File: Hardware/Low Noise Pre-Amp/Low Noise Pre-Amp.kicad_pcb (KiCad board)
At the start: 2 copper layers, 100 x 50 mm, 58 parts, among them J1 RF2-152-T-00-50-G-HDW, J2 RF2-152-T-00-50-G-HDW, J3 RF2-152-T-00-50-G-HDW, J4 WM4111-ND, U1 ADA4841-2, U2 LTC3260xMSE, U3 ADA4841-2, U4 L78L05_SOT89, U5 L79L05

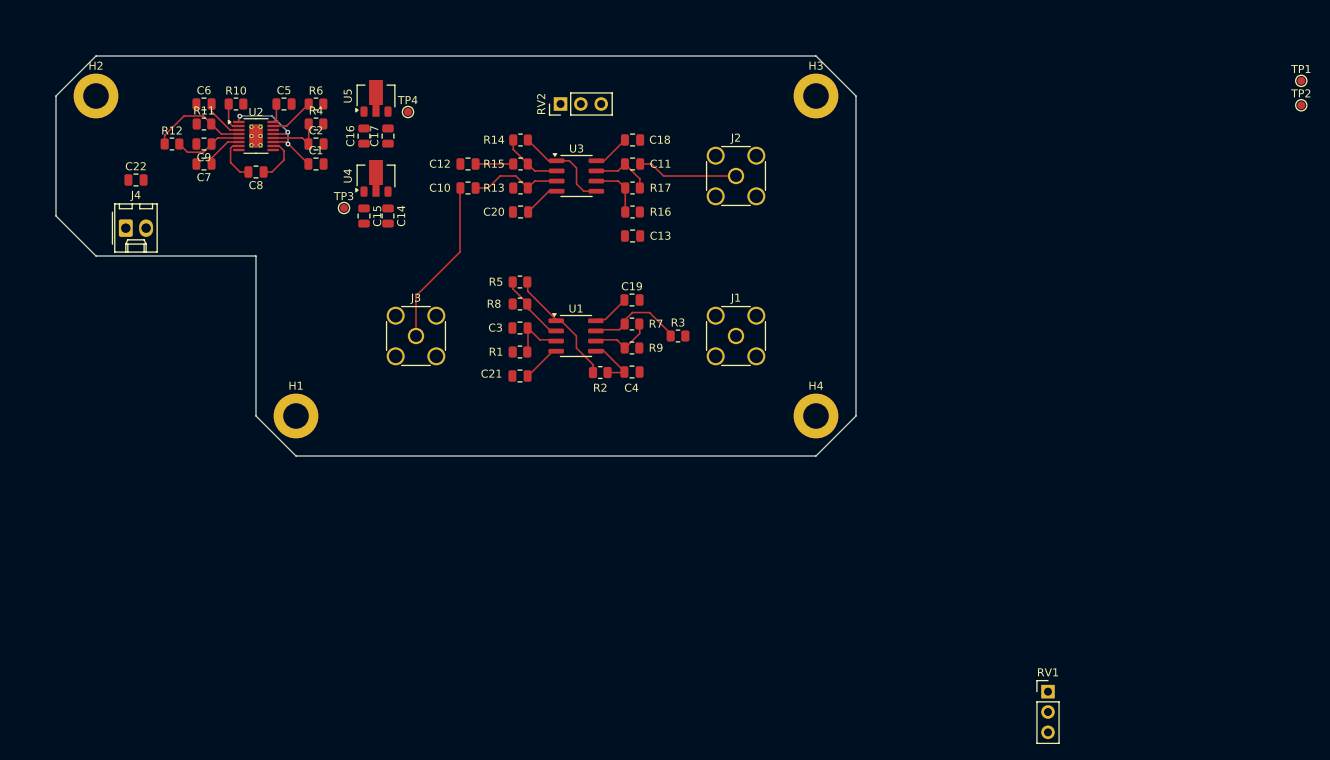
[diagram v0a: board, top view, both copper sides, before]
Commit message: Finalizing board layout
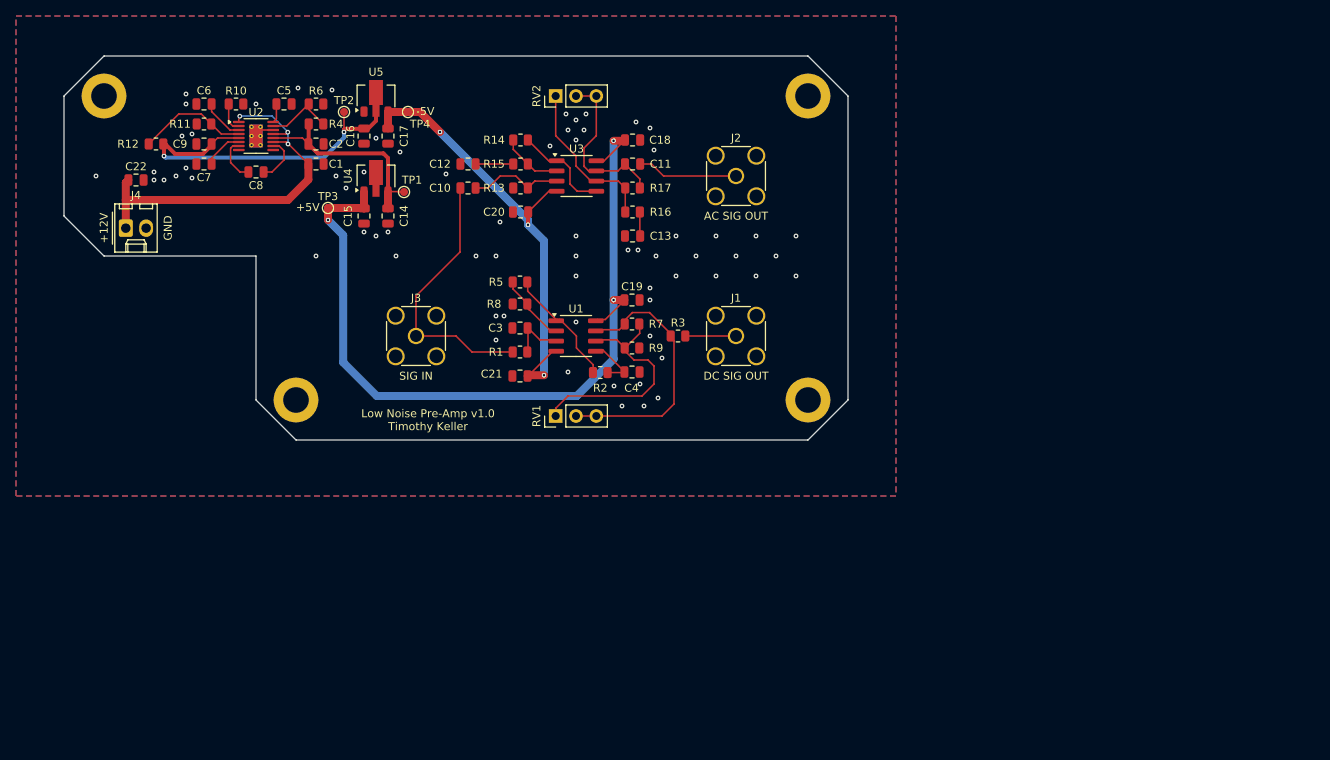
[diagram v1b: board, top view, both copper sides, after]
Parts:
- moved TP2 119.7 mm to (86.0, 57.0)
- moved TP1 113.0 mm to (93.5, 67.0)
- moved RV1 70.5 mm to (112.5, 95.0), turned to 90 degrees
- moved H4 2.24 mm to (144.0, 93.0)
- moved H1 2.00 mm to (80.0, 93.0)
- moved R12 2.00 mm to (62.5, 61.0)
- moved TP3 2.00 mm to (84.0, 69.0)
- moved RV2 1.17 mm to (112.5, 55.0)
- moved H2 1.00 mm to (56.0, 55.0)
- moved H3 1.00 mm to (144.0, 55.0)
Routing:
- net +5V: track 9.33 -> 103.6 mm, vias 0 -> 3
- net -5V: track 9.63 -> 58.8 mm, vias 0 -> 3
- net -7.2V: track 8.60 -> 45.2 mm, vias 0 -> 2
- net +12V: track 16.6 -> 48.6 mm
- net Net-(U1B--): track 7.96 -> 29.5 mm
- net Net-(R3-Pad1): track 12.0 -> 33.5 mm
- net +7.2V: track 7.23 -> 26.2 mm
- net Net-(C11-Pad1): track 7.70 -> 21.5 mm
- net Net-(U3B--): track 6.97 -> 20.1 mm
- net SIG_IN: track 20.9 -> 33.8 mm
- net SIG_DC_OUT: track 0.00 -> 6.34 mm
- net Net-(U2-ADJ^{+}): track 5.58 -> 8.83 mm
- net Net-(C13-Pad1): track 0.00 -> 3.02 mm
- net GND: track 0.00 -> 2.46 mm, vias 0 -> 69
- net Net-(U2-ADJ^{-}): track 12.3 -> 13.9 mm
- added copper zone on B.Cu, net GND
- added copper zone on F.Cu, net GND
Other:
- board size 100 x 50 mm -> 98 x 48 mm
- board text added: "${TITLE} ${REVISION} ${COMMENT1}"
- board text added: "+12V"
- board text added: "+5V"
- board text added: "-5V"
- board text added: "AC SIG OUT"
- board text added: "DC SIG OUT"
- board text added: "GND"
- board text added: "SIG IN"

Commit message: Minor changes to Pre amp
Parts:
- removed the H3 at (144.0, 55.0)
- R12, R4: value 500k -> 510k
- moved H1 74.4 mm to (144.0, 55.0)
- moved R3 1.52 mm to (128.0, 83.5)
- renumbered C8 to C10, C9 to C11, C10 to C12, C11 to C13, C18 to C14, C20 to C15, C12 to C16, C13 to C17, C14 to C18, C15 to C19, C16 to C20, C17 to C21, C19 to C3, C3 to C4, C4 to C5, C21 to C6, C5 to C7, C6 to C8, C7 to C9, H4 to H3
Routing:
- net +5V: track 103.6 -> 101.0 mm
- net Net-(R3-Pad1): track 33.5 -> 34.4 mm
- net GND: vias 69 -> 68
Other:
- outline, holes or cut-outs redrawn
